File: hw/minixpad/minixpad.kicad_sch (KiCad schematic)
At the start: 9 parts, among them J1 COM-09032, U1 NodeMCU-12K, U2 MicroUSB

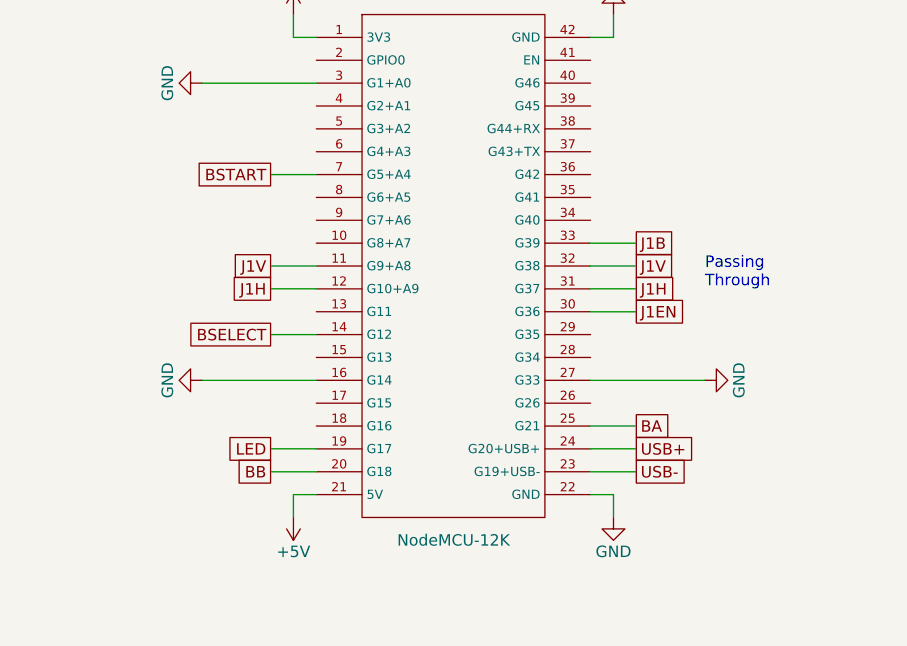
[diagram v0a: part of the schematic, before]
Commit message: Fix button numbering
Signed-off-by: Jan Hamal Dvořák <mordae@anilinux.org>
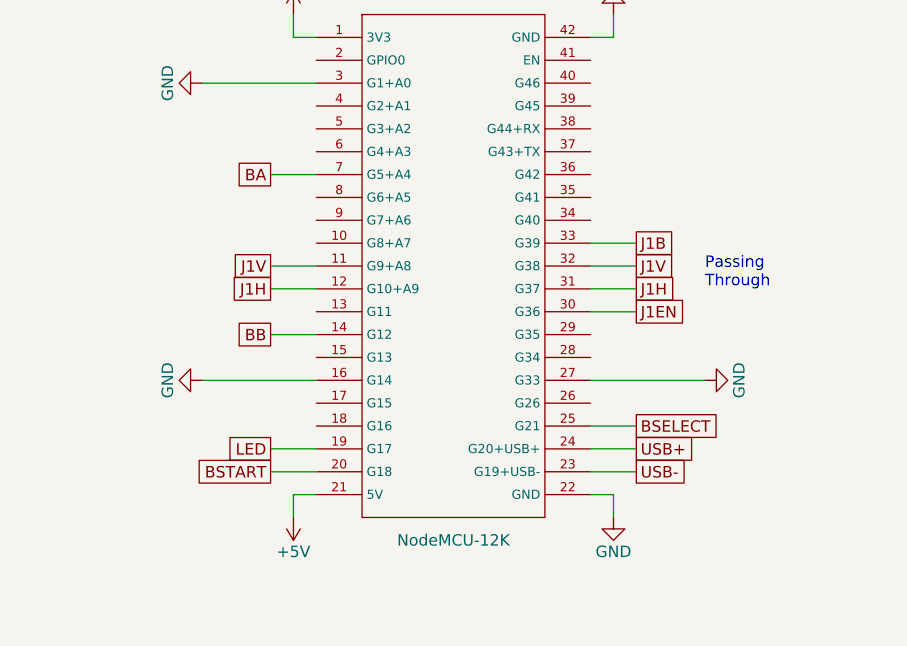
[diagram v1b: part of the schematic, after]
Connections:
- net BA: now also U1.7 (G5+A4); no longer U1.25 (G21)
- net BB: now also U1.14 (G12); no longer U1.20 (G18)
- net BSELECT: now also U1.25 (G21); no longer U1.14 (G12)
- net BSTART: now also U1.20 (G18); no longer U1.7 (G5+A4)
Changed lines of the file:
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@@
     )
   )
-  (global_label "BB" (shape passive) (at 116.84 142.24 180) (fields_autoplaced)
+  (global_label "BB" (shape passive) (at 116.84 127 180) (fields_autoplaced)
     (effects (font (size 1.27 1.27)) (justify right))
-    (property "Intersheet References" "${INTERSHEET_REFS}" (id 0) (at 111.8869 142.1606 0)
+    (property "Intersheet References" "${INTERSHEET_REFS}" (id 0) (at 111.8869 126.9206 0)
       (effects (font (size 1.27 1.27)) (justify right) hide)
     )
@@
     )
   )
-  (global_label "BA" (shape passive) (at 157.48 137.16 0) (fields_autoplaced)
-    (effects (font (size 1.27 1.27)) (justify left))
-    (property "Intersheet References" "${INTERSHEET_REFS}" (id 0) (at 162.2517 137.0806 0)
-      (effects (font (size 1.27 1.27)) (justify left) hide)
+  (global_label "BA" (shape passive) (at 116.84 109.22 180) (fields_autoplaced)
+    (effects (font (size 1.27 1.27)) (justify right))
+    (property "Intersheet References" "${INTERSHEET_REFS}" (id 0) (at 112.0683 109.2994 0)
+      (effects (font (size 1.27 1.27)) (justify right) hide)
     )
   )
@@
     )
   )
-  (global_label "BSELECT" (shape passive) (at 116.84 127 180) (fields_autoplaced)
-    (effects (font (size 1.27 1.27)) (justify right))
-    (property "Intersheet References" "${INTERSHEET_REFS}" (id 0) (at 106.3836 126.9206 0)
-      (effects (font (size 1.27 1.27)) (justify right) hide)
+  (global_label "BSELECT" (shape passive) (at 157.48 137.16 0) (fields_autoplaced)
+    (effects (font (size 1.27 1.27)) (justify left))
+    (property "Intersheet References" "${INTERSHEET_REFS}" (id 0) (at 167.9364 137.2394 0)
+      (effects (font (size 1.27 1.27)) (justify left) hide)
     )
   )
@@
     )
   )
-  (global_label "BSTART" (shape passive) (at 116.84 109.22 180) (fields_autoplaced)
+  (global_label "BSTART" (shape passive) (at 116.84 142.24 180) (fields_autoplaced)
     (effects (font (size 1.27 1.27)) (justify right))
-    (property "Intersheet References" "${INTERSHEET_REFS}" (id 0) (at 107.6536 109.2994 0)
+    (property "Intersheet References" "${INTERSHEET_REFS}" (id 0) (at 107.6536 142.3194 0)
       (effects (font (size 1.27 1.27)) (justify right) hide)
     )

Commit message: Revisit board designs
Signed-off-by: Jan Hamal Dvořák <mordae@anilinux.org>
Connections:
- net BA: now also B1.2 (B), B1.3 (B); no longer B3.2 (B), B3.3 (B)
- net BB: now also B2.2 (B), B2.3 (B); no longer B4.2 (B), B4.3 (B)
- net BSELECT: now also B3.2 (B), B3.3 (B); no longer B2.2 (B), B2.3 (B)
- net BSTART: now also B4.2 (B), B4.3 (B); no longer B1.2 (B), B1.3 (B)
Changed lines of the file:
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@@
     )
   )
-  (global_label "BSELECT" (shape passive) (at 177.8 25.4 0) (fields_autoplaced)
+  (global_label "BSELECT" (shape passive) (at 132.08 45.72 0) (fields_autoplaced)
     (effects (font (size 1.27 1.27)) (justify left))
-    (property "Intersheet References" "${INTERSHEET_REFS}" (id 0) (at 188.2564 25.3206 0)
+    (property "Intersheet References" "${INTERSHEET_REFS}" (id 0) (at 142.5364 45.6406 0)
       (effects (font (size 1.27 1.27)) (justify left) hide)
     )
@@
     )
   )
-  (global_label "BA" (shape passive) (at 132.08 45.72 0) (fields_autoplaced)
+  (global_label "BA" (shape passive) (at 132.08 25.4 0) (fields_autoplaced)
     (effects (font (size 1.27 1.27)) (justify left))
-    (property "Intersheet References" "${INTERSHEET_REFS}" (id 0) (at 136.8517 45.6406 0)
+    (property "Intersheet References" "${INTERSHEET_REFS}" (id 0) (at 136.8517 25.3206 0)
       (effects (font (size 1.27 1.27)) (justify left) hide)
     )
   )
-  (global_label "BB" (shape passive) (at 177.8 45.72 0) (fields_autoplaced)
+  (global_label "BB" (shape passive) (at 177.8 25.4 0) (fields_autoplaced)
     (effects (font (size 1.27 1.27)) (justify left))
-    (property "Intersheet References" "${INTERSHEET_REFS}" (id 0) (at 182.7531 45.6406 0)
+    (property "Intersheet References" "${INTERSHEET_REFS}" (id 0) (at 182.7531 25.3206 0)
       (effects (font (size 1.27 1.27)) (justify left) hide)
     )
@@
     )
   )
-  (global_label "BSTART" (shape passive) (at 132.08 25.4 0) (fields_autoplaced)
+  (global_label "BSTART" (shape passive) (at 177.8 45.72 0) (fields_autoplaced)
     (effects (font (size 1.27 1.27)) (justify left))
-    (property "Intersheet References" "${INTERSHEET_REFS}" (id 0) (at 141.2664 25.3206 0)
+    (property "Intersheet References" "${INTERSHEET_REFS}" (id 0) (at 186.9864 45.6406 0)
       (effects (font (size 1.27 1.27)) (justify left) hide)
     )
